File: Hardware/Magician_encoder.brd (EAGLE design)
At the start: 21.6 x 39.4 mm, 29 parts, among them Q1 MMBT2222A, Q2 MMBT2222A, U1 QRE1113, U2 QRE1113

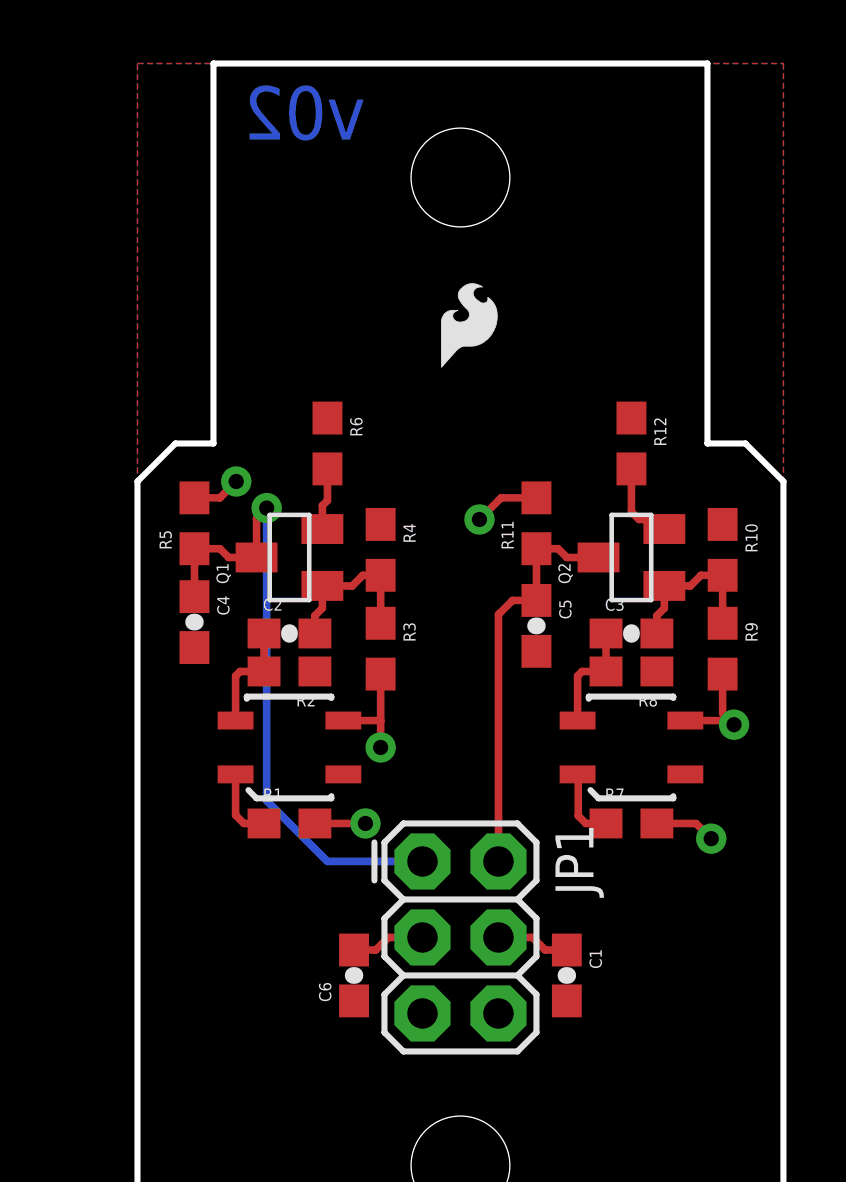
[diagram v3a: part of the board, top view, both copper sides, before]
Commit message: Update values and circuit for better performance
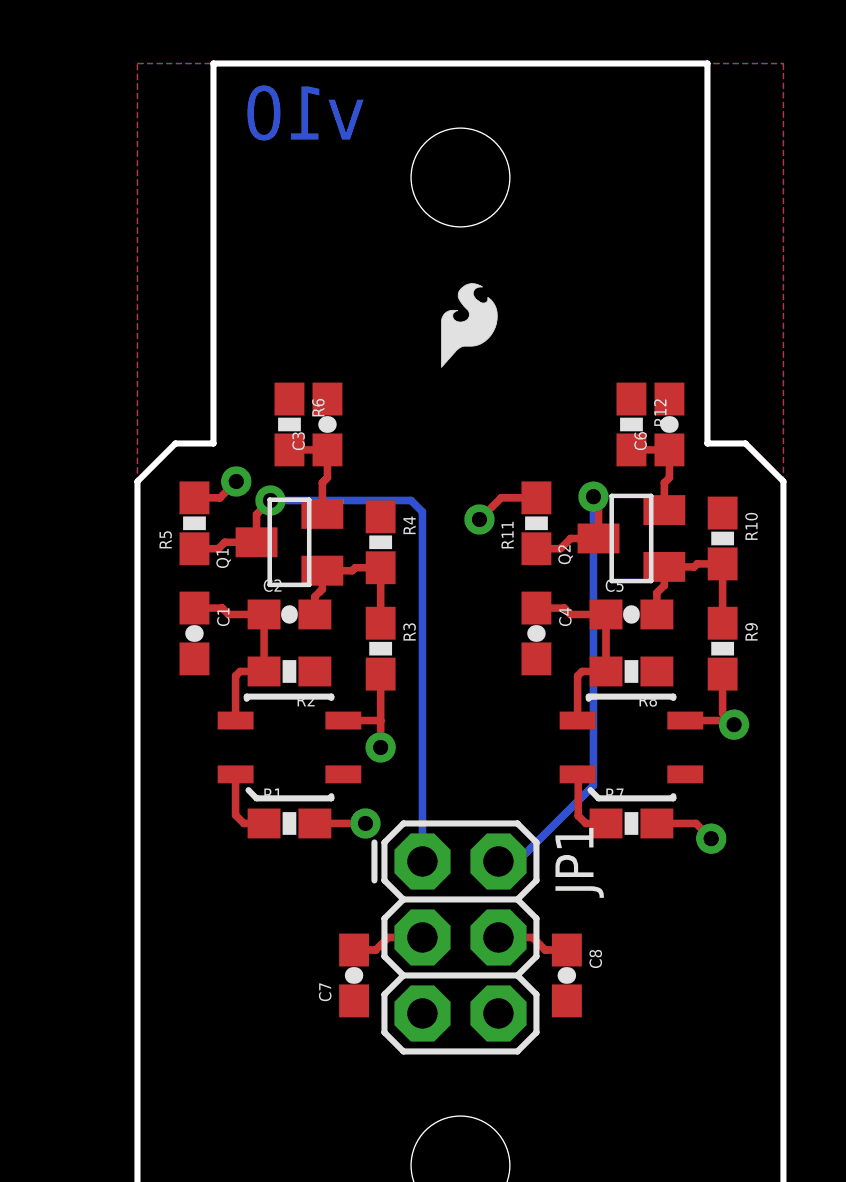
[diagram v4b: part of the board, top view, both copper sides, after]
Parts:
- added C7: 1.0uF, SparkFun-Capacitors:0603-CAP
- added C8: 0.1uF, SparkFun-Capacitors:0603-CAP
- C3, C6: value 1.0uF -> 0.1uF
- C5: value 0.1uF -> 1.0uF
- R1, R10, R11, R3, R4, R5, R7, R9: device SparkFun-Resistors:0603 -> SparkFun-Resistors:0603-RES
- R12, R6: value 680 -> 1K; device SparkFun-Resistors:0603 -> SparkFun-Resistors:0603-RES
- R2, R8: value 1K -> 10K; device SparkFun-Resistors:0603 -> SparkFun-Resistors:0603-RES
- moved C6 21.2 mm to (17.8, 27.3)
- moved C1 16.9 mm to (1.91, 20.3)
- moved C3 12.3 mm to (6.35, 27.3), turned to 90 degrees
- moved C4 11.4 mm to (13.3, 20.3)
- moved C5 3.20 mm to (16.5, 21.0), turned to 0 degrees
- moved R6 1.42 mm to (5.08, 27.3)
- moved Q2 0.64 mm to (16.5, 23.5)
- moved C2 0.63 mm to (5.08, 21.0)
- moved R12 0.63 mm to (16.5, 27.3)
- moved Q1 0.51 mm to (5.08, 23.4)
- moved R10 0.38 mm to (19.6, 23.5)
- moved R4 0.25 mm to (8.13, 23.4)
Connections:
- net 5V: now also C7.2, C8.1; no longer C1.1, C6.2
- net GND: now also C3.2, C6.2, C7.1, C8.2; no longer C5.2, C6.1
- net N$1: now also C1.1
- net N$3: now also C3.1
- net N$7: now also C6.1
- net N$8: now also C4.1, C5.1; no longer C3.1
- net N$9: now also C5.2; no longer C3.2
- net OUTA: no longer C4.1
- net OUTB: no longer C5.1
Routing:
- net OUTB: track 13.6 -> 17.6 mm, vias 0 -> 1
- net N$1: track 3.77 -> 6.82 mm
- net N$8: track 3.77 -> 6.82 mm
- net N$3: track 2.08 -> 3.48 mm
- net OUTA: track 21.4 -> 20.7 mm
- net N$9: track 5.39 -> 6.06 mm
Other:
- board text added: "v10"
- board text removed: "v02"

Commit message: Update schematic with prod. values
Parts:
- R10, R4: value 10K -> 6.8K
- R11, R5: value 10K -> 4.7K
- R12, R6: value 1K -> 100
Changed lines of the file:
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@@
 <layers>
 <layer number="1" name="Top" color="4" fill="1" visible="yes" active="yes"/>
-<layer number="2" name="Route2" color="1" fill="3" visible="yes" active="yes"/>
-<layer number="15" name="Route15" color="4" fill="6" visible="yes" active="yes"/>
+<layer number="2" name="Route2" color="1" fill="3" visible="no" active="yes"/>
+<layer number="15" name="Route15" color="4" fill="6" visible="no" active="yes"/>
 <layer number="16" name="Bottom" color="1" fill="1" visible="yes" active="yes"/>
 <layer number="17" name="Pads" color="2" fill="1" visible="yes" active="yes"/>
@@
 <layer number="23" name="tOrigins" color="15" fill="1" visible="yes" active="yes"/>
 <layer number="24" name="bOrigins" color="15" fill="1" visible="yes" active="yes"/>
-<layer number="25" name="tNames" color="7" fill="1" visible="yes" active="yes"/>
-<layer number="26" name="bNames" color="7" fill="1" visible="yes" active="yes"/>
-<layer number="27" name="tValues" color="7" fill="1" visible="yes" active="yes"/>
-<layer number="28" name="bValues" color="7" fill="1" visible="yes" active="yes"/>
-<layer number="29" name="tStop" color="7" fill="3" visible="yes" active="yes"/>
-<layer number="30" name="bStop" color="7" fill="6" visible="yes" active="yes"/>
-<layer number="31" name="tCream" color="7" fill="4" visible="yes" active="yes"/>
-<layer number="32" name="bCream" color="7" fill="5" visible="yes" active="yes"/>
-<layer number="39" name="tKeepout" color="4" fill="11" visible="yes" active="yes"/>
-<layer number="40" name="bKeepout" color="1" fill="11" visible="yes" active="yes"/>
-<layer number="41" name="tRestrict" color="4" fill="10" visible="yes" active="yes"/>
-<layer number="42" name="bRestrict" color="1" fill="10" visible="yes" active="yes"/>
-<layer number="44" name="Drills" color="7" fill="1" visible="yes" active="yes"/>
+<layer number="25" name="tNames" color="7" fill="1" visible="no" active="yes"/>
+<layer number="26" name="bNames" color="7" fill="1" visible="no" active="yes"/>
+<layer number="27" name="tValues" color="7" fill="1" visible="no" active="yes"/>
+<layer number="28" name="bValues" color="7" fill="1" visible="no" active="yes"/>
+<layer number="29" name="tStop" color="7" fill="3" visible="no" active="yes"/>
+<layer number="30" name="bStop" color="7" fill="6" visible="no" active="yes"/>
+<layer number="31" name="tCream" color="7" fill="4" visible="no" active="yes"/>
+<layer number="32" name="bCream" color="7" fill="5" visible="no" active="yes"/>
+<layer number="39" name="tKeepout" color="4" fill="11" visible="no" active="yes"/>
+<layer number="40" name="bKeepout" color="1" fill="11" visible="no" active="yes"/>
+<layer number="41" name="tRestrict" color="4" fill="10" visible="no" active="yes"/>
+<layer number="42" name="bRestrict" color="1" fill="10" visible="no" active="yes"/>
+<layer number="43" name="vRestrict" color="2" fill="10" visible="no" active="yes"/>
+<layer number="44" name="Drills" color="7" fill="1" visible="no" active="yes"/>
 <layer number="45" name="Holes" color="7" fill="1" visible="yes" active="yes"/>
-<layer number="46" name="Milling" color="3" fill="1" visible="yes" active="yes"/>
+<layer number="46" name="Milling" color="3" fill="1" visible="no" active="yes"/>
 <layer number="51" name="tDocu" color="6" fill="1" visible="yes" active="yes"/>
-<layer number="52" name="bDocu" color="7" fill="1" visible="yes" active="yes"/>
+<layer number="52" name="bDocu" color="7" fill="1" visible="no" active="yes"/>
 <layer number="3" name="Route3" color="4" fill="3" visible="no" active="no"/>
 <layer number="4" name="Route4" color="1" fill="4" visible="no" active="no"/>
@@
 <layer number="37" name="tTest" color="7" fill="1" visible="no" active="no"/>
 <layer number="38" name="bTest" color="7" fill="1" visible="no" active="no"/>
-<layer number="43" name="vRestrict" color="2" fill="10" visible="no" active="no"/>
 <layer number="47" name="Measures" color="7" fill="1" visible="no" active="no"/>
 <layer number="48" name="Document" color="7" fill="1" visible="no" active="no"/>
@@
 <attribute name="PROD_ID" value="RES-07871" x="8.128" y="19.812" size="1.778" layer="27" font="vector" ratio="15" rot="R270" display="off"/>
 </element>
-<element name="R4" library="SparkFun-Resistors" package="0603-RES" value="10K" x="8.128" y="23.368" rot="R270">
-<attribute name="PROD_ID" value="RES-00824" x="8.128" y="23.368" size="1.778" layer="27" font="vector" ratio="15" rot="R270" display="off"/>
-</element>
-<element name="R5" library="SparkFun-Resistors" package="0603-RES" value="10K" x="1.905" y="24.003" rot="R90">
-<attribute name="PROD_ID" value="RES-00824" x="1.905" y="24.003" size="1.778" layer="27" font="vector" ratio="15" rot="R90" display="off"/>
-</element>
-<element name="R12" library="SparkFun-Resistors" package="0603-RES" value="1K" x="16.51" y="27.305" rot="R270">
-<attribute name="PROD_ID" value="RES-07856" x="16.51" y="27.305" size="1.778" layer="27" font="vector" ratio="15" rot="R270" display="off"/>
+<element name="R4" library="SparkFun-Resistors" package="0603-RES" value="6.8K" x="8.128" y="23.368" rot="R270">
+<attribute name="PROD_ID" value="RES-08597" x="8.128" y="23.368" size="1.778" layer="27" font="vector" ratio="15" rot="R270" display="off"/>
+</element>
+<element name="R5" library="SparkFun-Resistors" package="0603-RES" value="4.7K" x="1.905" y="24.003" rot="R90">
+<attribute name="PROD_ID" value="RES-07857" x="1.905" y="24.003" size="1.778" layer="27" font="vector" ratio="15" rot="R90" display="off"/>
+</element>
+<element name="R12" library="SparkFun-Resistors" package="0603-RES" value="100" x="16.51" y="27.305" rot="R270">
+<attribute name="PROD_ID" value="RES-07863" x="16.51" y="27.305" size="1.778" layer="27" font="vector" ratio="15" rot="R270" display="off"/>
 </element>
 <element name="C5" library="SparkFun-Capacitors" package="0603-CAP" value="1.0uF" x="16.51" y="20.955">
@@
 <attribute name="PROD_ID" value="RES-07871" x="19.558" y="19.812" size="1.778" layer="27" font="vector" ratio="15" rot="R270" display="off"/>
 </element>
-<element name="R10" library="SparkFun-Resistors" package="0603-RES" value="10K" x="19.558" y="23.495" rot="R270">
-<attribute name="PROD_ID" value="RES-00824" x="19.558" y="23.495" size="1.778" layer="27" font="vector" ratio="15" rot="R270" display="off"/>
-</element>
-<element name="R11" library="SparkFun-Resistors" package="0603-RES" value="10K" x="13.335" y="24.003" rot="R90">
-<attribute name="PROD_ID" value="RES-00824" x="13.335" y="24.003" size="1.778" layer="27" font="vector" ratio="15" rot="R90" display="off"/>
+<element name="R10" library="SparkFun-Resistors" package="0603-RES" value="6.8K" x="19.558" y="23.495" rot="R270">
+<attribute name="PROD_ID" value="RES-08597" x="19.558" y="23.495" size="1.778" layer="27" font="vector" ratio="15" rot="R270" display="off"/>
+</element>
+<element name="R11" library="SparkFun-Resistors" package="0603-RES" value="4.7K" x="13.335" y="24.003" rot="R90">
+<attribute name="PROD_ID" value="RES-07857" x="13.335" y="24.003" size="1.778" layer="27" font="vector" ratio="15" rot="R90" display="off"/>
 </element>
 <element name="C3" library="SparkFun-Capacitors" package="0603-CAP" value="0.1uF" x="6.35" y="27.305" rot="R90">
@@
 </element>
 <element name="LOGO1" library="SparkFun-Aesthetics" package="SFE-LOGO-FLAME" value="LOGO-SFESK" x="10.16" y="29.21"/>
-<element name="R6" library="SparkFun-Resistors" package="0603-RES" value="1K" x="5.08" y="27.305" rot="R270">
-<attribute name="PROD_ID" value="RES-07856" x="5.08" y="27.305" size="1.778" layer="27" font="vector" ratio="15" rot="R270" display="off"/>
+<element name="R6" library="SparkFun-Resistors" package="0603-RES" value="100" x="5.08" y="27.305" rot="R270">
+<attribute name="PROD_ID" value="RES-07863" x="5.08" y="27.305" size="1.778" layer="27" font="vector" ratio="15" rot="R270" display="off"/>
 </element>
 <element name="R2" library="SparkFun-Resistors" package="0603-RES" value="10K" x="5.08" y="19.05" rot="R180">
